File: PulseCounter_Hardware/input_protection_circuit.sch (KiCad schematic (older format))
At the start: 193 parts, among them J1 Conn_01x32_Male, U34 LTV-817, U35 LTV-817, U36 LTV-817, U37 LTV-817, U38 LTV-817, U39 LTV-817, U40 LTV-817, U41 LTV-817, U42 LTV-817, U43 LTV-817, U44 LTV-817, U45 LTV-817, U46 LTV-817, U47 LTV-817, U48 LTV-817, U49 LTV-817, U50 LTV-817, U51 LTV-817, U52 LTV-817, U53 LTV-817, U54 LTV-817, U55 LTV-817, U56 LTV-817, U57 LTV-817, U58 LTV-817, U59 LTV-817, U60 LTV-817, U61 LTV-817, U62 LTV-817, U63 LTV-817, U64 LTV-817, U65 LTV-817

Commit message: Starting with MCU
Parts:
- removed J1: Conn_01x32_Male, symbol Connector:Conn_01x32_Male
- added J1: Conn_01x33_Female, symbol Connector:Conn_01x33_Female
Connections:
- net CHANNEL_IN_0: now also J1.1 (Pin_1)
- net CHANNEL_IN_1: now also J1.2 (Pin_2)
- net CHANNEL_IN_10: now also J1.11 (Pin_11)
- net CHANNEL_IN_11: now also J1.12 (Pin_12)
- net CHANNEL_IN_12: now also J1.13 (Pin_13)
- net CHANNEL_IN_13: now also J1.14 (Pin_14)
- net CHANNEL_IN_14: now also J1.15 (Pin_15)
- net CHANNEL_IN_15: now also J1.16 (Pin_16)
- net CHANNEL_IN_16: now also J1.17 (Pin_17)
- net CHANNEL_IN_17: now also J1.18 (Pin_18)
- net CHANNEL_IN_18: now also J1.19 (Pin_19)
- net CHANNEL_IN_19: now also J1.20 (Pin_20)
- net CHANNEL_IN_2: now also J1.3 (Pin_3)
- net CHANNEL_IN_20: now also J1.21 (Pin_21)
- net CHANNEL_IN_21: now also J1.22 (Pin_22)
- net CHANNEL_IN_22: now also J1.23 (Pin_23)
- net CHANNEL_IN_23: now also J1.24 (Pin_24)
- net CHANNEL_IN_24: now also J1.25 (Pin_25)
- net CHANNEL_IN_25: now also J1.26 (Pin_26)
- net CHANNEL_IN_26: now also J1.27 (Pin_27)
- net CHANNEL_IN_27: now also J1.28 (Pin_28)
- net CHANNEL_IN_28: now also J1.29 (Pin_29)
- net CHANNEL_IN_29: now also J1.30 (Pin_30)
- net CHANNEL_IN_3: now also J1.4 (Pin_4)
- net CHANNEL_IN_30: now also J1.31 (Pin_31)
- net CHANNEL_IN_31: now also J1.32 (Pin_32)
- net CHANNEL_IN_4: now also J1.5 (Pin_5)
- net CHANNEL_IN_5: now also J1.6 (Pin_6)
- net CHANNEL_IN_6: now also J1.7 (Pin_7)
- net CHANNEL_IN_7: now also J1.8 (Pin_8)
- net CHANNEL_IN_8: now also J1.9 (Pin_9)
- net CHANNEL_IN_9: now also J1.10 (Pin_10)
- net OPTO_GND: now also J1.33 (Pin_33)
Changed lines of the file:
@@
 Wire Wire Line
 	13550 2400 13800 2400
-$Comp
-L Connector:Conn_01x32_Male J1
-U 1 1 5FA21E59
-P 14000 3900
-F 0 "J1" H 13972 3874 50  0000 R CNN
-F 1 "Conn_01x32_Male" H 13972 3783 50  0000 R CNN
-F 2 "" H 14000 3900 50  0001 C CNN
-F 3 "~" H 14000 3900 50  0001 C CNN
-	1    14000 3900
-	-1   0    0    -1
-$EndComp
 Wire Wire Line
 	13800 2500 13550 2500
@@
 Wire Notes Line
 	6850 800  6850 10750
+$Comp
+L Connector:Conn_01x33_Female J1
+U 1 1 5FD194EE
+P 14000 4000
+F 0 "J1" H 14028 4026 50  0000 L CNN
+F 1 "Conn_01x33_Female" H 14028 3935 50  0000 L CNN
+F 2 "" H 14000 4000 50  0001 C CNN
+F 3 "~" H 14000 4000 50  0001 C CNN
+	1    14000 4000
+	1    0    0    -1
+$EndComp
+Text Label 13550 5600 2    50   ~ 0
+OPTO_GND
+Wire Wire Line
+	13550 5600 13800 5600
+Text Label 13500 6050 2    50   ~ 0
+GND
+Text Label 13500 5950 2    50   ~ 0
+3V3
+Text HLabel 13700 6050 2    50   UnSpc ~ 0
+GND
+Text HLabel 13700 5950 2    50   UnSpc ~ 0
+3V3
+Wire Wire Line
+	13700 5950 13500 5950
+Wire Wire Line
+	13500 6050 13700 6050
 $EndSCHEMATC

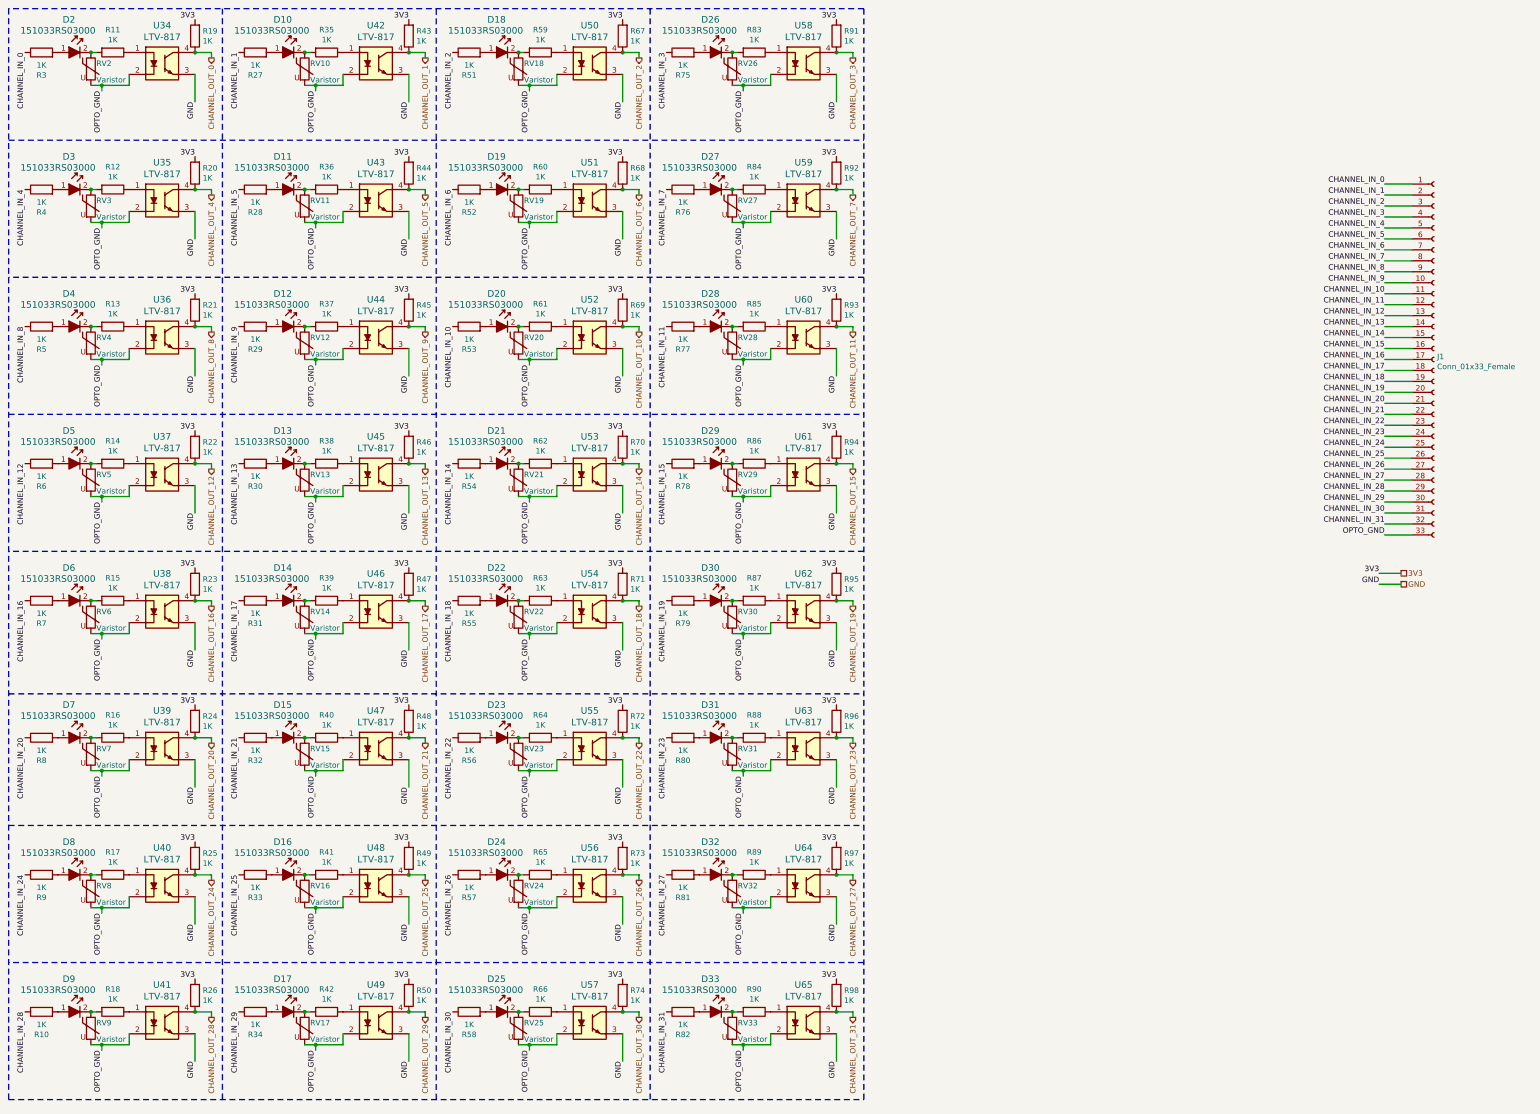
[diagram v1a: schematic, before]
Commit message: Added SPI flash, connected I2C, SPI
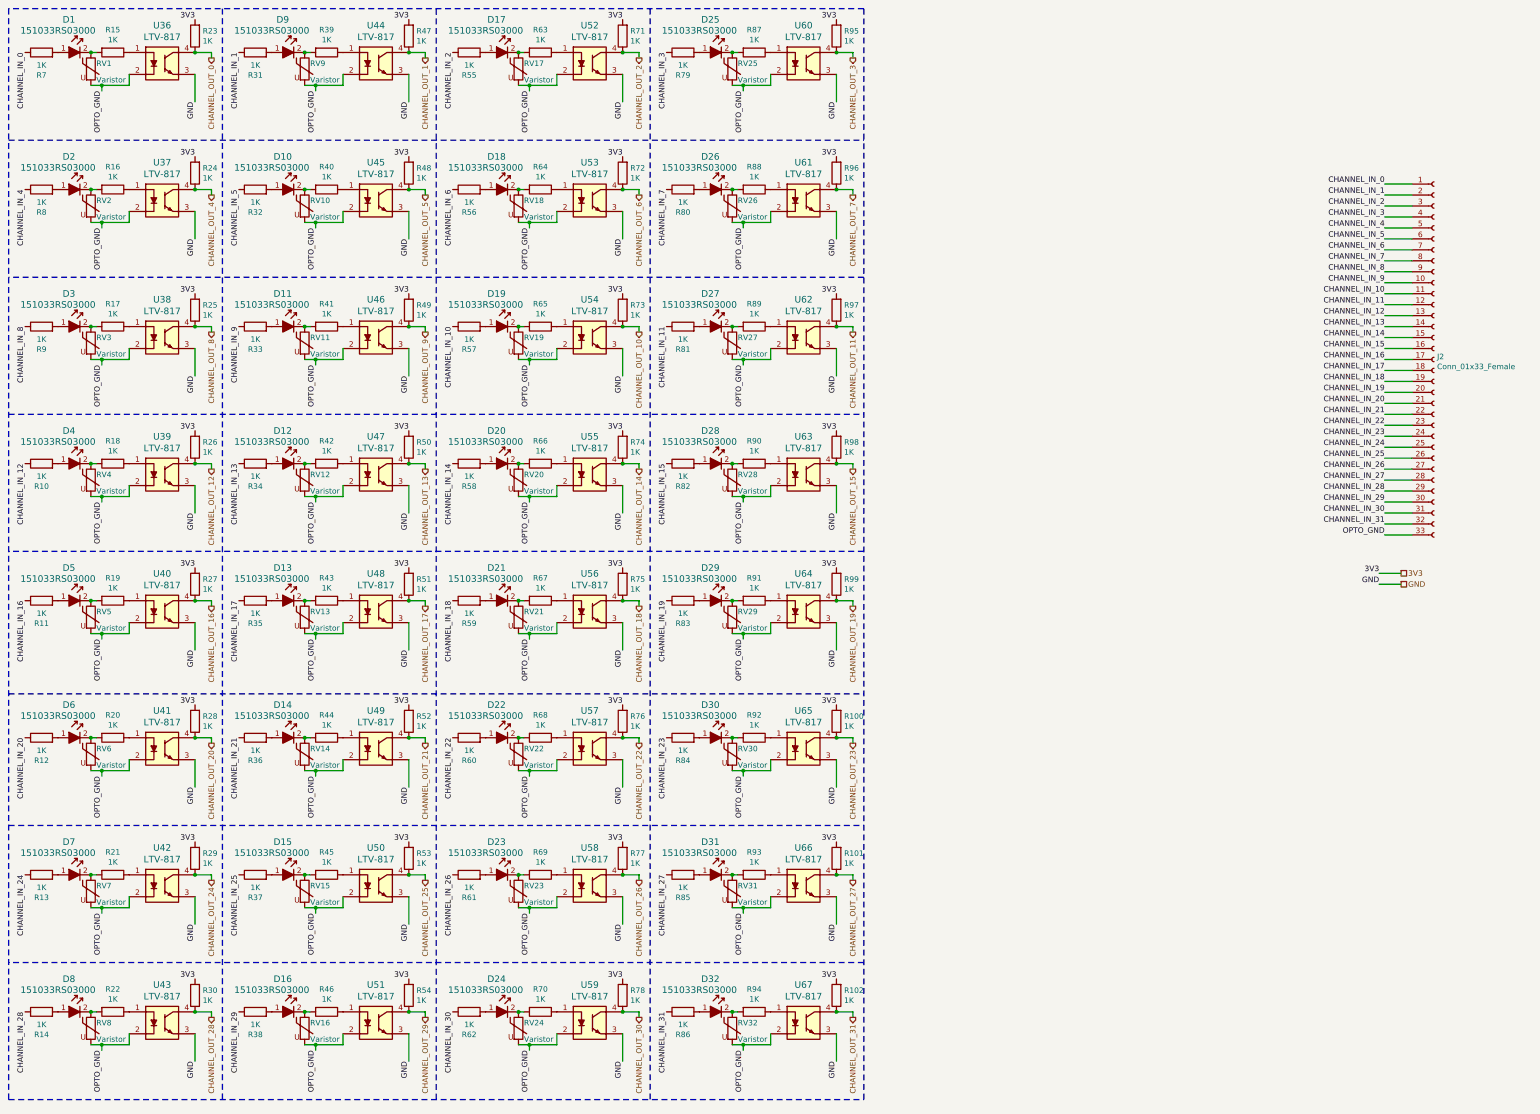
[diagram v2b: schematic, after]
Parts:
- renumbered D2 to D1, D11 to D10, D12 to D11, D13 to D12, D14 to D13, D15 to D14, D16 to D15, D17 to D16, D18 to D17, D19 to D18, D20 to D19, D3 to D2, D21 to D20, D22 to D21, D23 to D22, D24 to D23, D25 to D24, D26 to D25, D27 to D26, D28 to D27, D29 to D28, D30 to D29, D4 to D3, D31 to D30, D32 to D31, D33 to D32, D5 to D4, D6 to D5, D7 to D6, D8 to D7, D9 to D8, D10 to D9, J1 to J2, R6 to R10, R96 to R100, R97 to R101, R98 to R102, R7 to R11, R8 to R12, R9 to R13, R10 to R14, R11 to R15, R12 to R16, R13 to R17, R14 to R18, R15 to R19, R16 to R20, R17 to R21, R18 to R22, R19 to R23, R20 to R24, R21 to R25, R22 to R26, R23 to R27, R24 to R28, R25 to R29, R26 to R30, R27 to R31, R28 to R32, R29 to R33, R30 to R34, R31 to R35, R32 to R36, R33 to R37, R34 to R38, R35 to R39, R36 to R40, R37 to R41, R38 to R42, R39 to R43, R40 to R44, R41 to R45, R42 to R46, R43 to R47, R44 to R48, R45 to R49, R46 to R50, R47 to R51, R48 to R52, R49 to R53, R50 to R54, R51 to R55, R52 to R56, R53 to R57, R54 to R58, R55 to R59, R56 to R60, R57 to R61, R58 to R62, R59 to R63, R60 to R64, R61 to R65, R62 to R66, R63 to R67, R64 to R68, R65 to R69, R3 to R7, R66 to R70, R67 to R71, R68 to R72, R69 to R73, R70 to R74, R71 to R75, R72 to R76, R73 to R77, R74 to R78, R75 to R79, R4 to R8, R76 to R80, R77 to R81, R78 to R82, R79 to R83, R80 to R84, R81 to R85, R82 to R86, R83 to R87, R84 to R88, R85 to R89, R5 to R9, R86 to R90, R87 to R91, R88 to R92, R89 to R93, R90 to R94, R91 to R95, R92 to R96, R93 to R97, R94 to R98, R95 to R99, RV2 to RV1, RV11 to RV10, RV12 to RV11, RV13 to RV12, RV14 to RV13, RV15 to RV14, RV16 to RV15, RV17 to RV16, RV18 to RV17, RV19 to RV18, RV20 to RV19, RV3 to RV2, RV21 to RV20, RV22 to RV21, RV23 to RV22, RV24 to RV23, RV25 to RV24, RV26 to RV25, RV27 to RV26, RV28 to RV27, RV29 to RV28, RV30 to RV29, RV4 to RV3, RV31 to RV30, RV32 to RV31, RV33 to RV32, RV5 to RV4, RV6 to RV5, RV7 to RV6, RV8 to RV7, RV9 to RV8, RV10 to RV9, U34 to U36, U35 to U37, U36 to U38, U37 to U39, U38 to U40, U39 to U41, U40 to U42, U41 to U43, U42 to U44, U43 to U45, U44 to U46, U45 to U47, U46 to U48, U47 to U49, U48 to U50, U49 to U51, U50 to U52, U51 to U53, U52 to U54, U53 to U55, U54 to U56, U55 to U57, U56 to U58, U57 to U59, U58 to U60, U59 to U61, U60 to U62, U61 to U63, U62 to U64, U63 to U65, U64 to U66, U65 to U67

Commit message: Added correct varistor
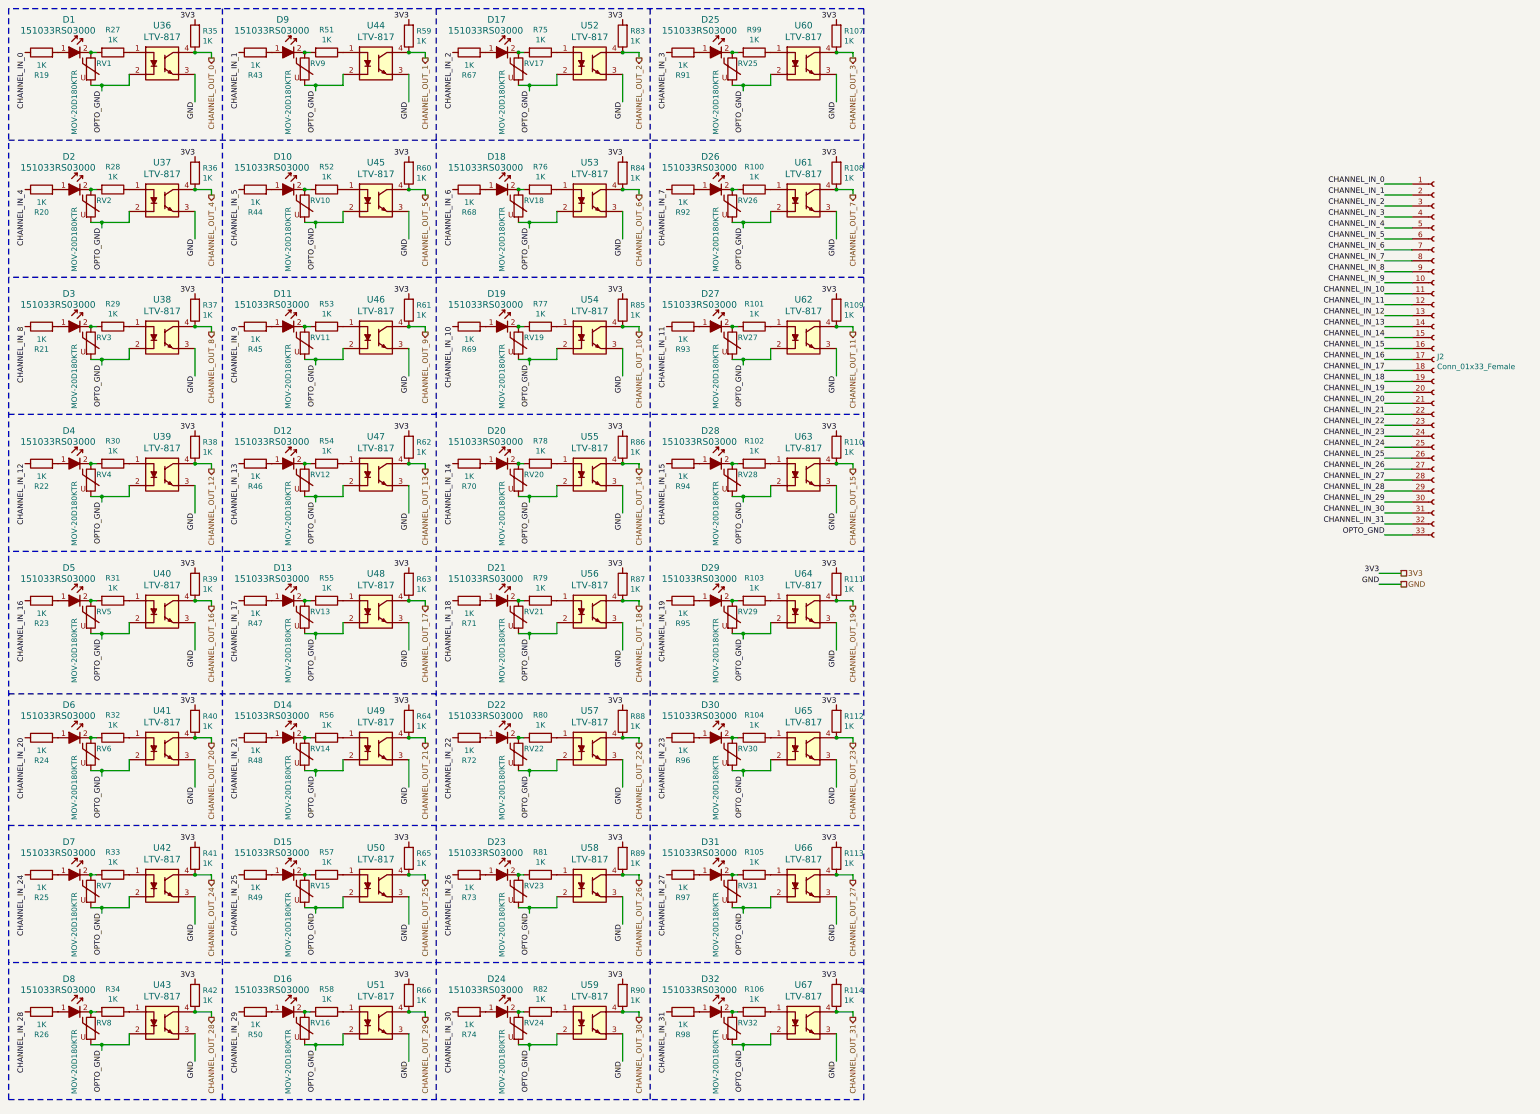
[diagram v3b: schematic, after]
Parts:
- J2: footprint (none) -> Connector_PinSocket_2.54mm:PinSocket_1x33_P2.54mm_Vertical
- R100: renamed from R88; footprint (none) -> Resistor_SMD:R_0603_1608Metric_Pad1.05x0.95mm_HandSolder
- R101: renamed from R89; footprint (none) -> Resistor_SMD:R_0603_1608Metric_Pad1.05x0.95mm_HandSolder
- R102: renamed from R90; footprint (none) -> Resistor_SMD:R_0603_1608Metric_Pad1.05x0.95mm_HandSolder
- R103: renamed from R91; footprint (none) -> Resistor_SMD:R_0603_1608Metric_Pad1.05x0.95mm_HandSolder
- R104: renamed from R92; footprint (none) -> Resistor_SMD:R_0603_1608Metric_Pad1.05x0.95mm_HandSolder
- R105: renamed from R93; footprint (none) -> Resistor_SMD:R_0603_1608Metric_Pad1.05x0.95mm_HandSolder
- R106: renamed from R94; footprint (none) -> Resistor_SMD:R_0603_1608Metric_Pad1.05x0.95mm_HandSolder
- R107: renamed from R95; footprint (none) -> Resistor_SMD:R_0603_1608Metric_Pad1.05x0.95mm_HandSolder
- R108: renamed from R96; footprint (none) -> Resistor_SMD:R_0603_1608Metric_Pad1.05x0.95mm_HandSolder
- R109: renamed from R97; footprint (none) -> Resistor_SMD:R_0603_1608Metric_Pad1.05x0.95mm_HandSolder
- R110: renamed from R98; footprint (none) -> Resistor_SMD:R_0603_1608Metric_Pad1.05x0.95mm_HandSolder
- R111: renamed from R99; footprint (none) -> Resistor_SMD:R_0603_1608Metric_Pad1.05x0.95mm_HandSolder
- R112: renamed from R100; footprint (none) -> Resistor_SMD:R_0603_1608Metric_Pad1.05x0.95mm_HandSolder
- R113: renamed from R101; footprint (none) -> Resistor_SMD:R_0603_1608Metric_Pad1.05x0.95mm_HandSolder
- R114: renamed from R102; footprint (none) -> Resistor_SMD:R_0603_1608Metric_Pad1.05x0.95mm_HandSolder
- R19: renamed from R7; footprint (none) -> Resistor_SMD:R_0603_1608Metric_Pad1.05x0.95mm_HandSolder
- R20: renamed from R8; footprint (none) -> Resistor_SMD:R_0603_1608Metric_Pad1.05x0.95mm_HandSolder
- R21: renamed from R9; footprint (none) -> Resistor_SMD:R_0603_1608Metric_Pad1.05x0.95mm_HandSolder
- R22: renamed from R10; footprint (none) -> Resistor_SMD:R_0603_1608Metric_Pad1.05x0.95mm_HandSolder
- R23: renamed from R11; footprint (none) -> Resistor_SMD:R_0603_1608Metric_Pad1.05x0.95mm_HandSolder
- R24: renamed from R12; footprint (none) -> Resistor_SMD:R_0603_1608Metric_Pad1.05x0.95mm_HandSolder
- R25: renamed from R13; footprint (none) -> Resistor_SMD:R_0603_1608Metric_Pad1.05x0.95mm_HandSolder
- R26: renamed from R14; footprint (none) -> Resistor_SMD:R_0603_1608Metric_Pad1.05x0.95mm_HandSolder
- R27: renamed from R15; footprint (none) -> Resistor_SMD:R_0603_1608Metric_Pad1.05x0.95mm_HandSolder
- R28: renamed from R16; footprint (none) -> Resistor_SMD:R_0603_1608Metric_Pad1.05x0.95mm_HandSolder
- R29: renamed from R17; footprint (none) -> Resistor_SMD:R_0603_1608Metric_Pad1.05x0.95mm_HandSolder
- R30: renamed from R18; footprint (none) -> Resistor_SMD:R_0603_1608Metric_Pad1.05x0.95mm_HandSolder
- R31: renamed from R19; footprint (none) -> Resistor_SMD:R_0603_1608Metric_Pad1.05x0.95mm_HandSolder
- R32: renamed from R20; footprint (none) -> Resistor_SMD:R_0603_1608Metric_Pad1.05x0.95mm_HandSolder
- R33: renamed from R21; footprint (none) -> Resistor_SMD:R_0603_1608Metric_Pad1.05x0.95mm_HandSolder
- R34: renamed from R22; footprint (none) -> Resistor_SMD:R_0603_1608Metric_Pad1.05x0.95mm_HandSolder
- R35: renamed from R23; footprint (none) -> Resistor_SMD:R_0603_1608Metric_Pad1.05x0.95mm_HandSolder
- R36: renamed from R24; footprint (none) -> Resistor_SMD:R_0603_1608Metric_Pad1.05x0.95mm_HandSolder
- R37: renamed from R25; footprint (none) -> Resistor_SMD:R_0603_1608Metric_Pad1.05x0.95mm_HandSolder
- R38: renamed from R26; footprint (none) -> Resistor_SMD:R_0603_1608Metric_Pad1.05x0.95mm_HandSolder
- R39: renamed from R27; footprint (none) -> Resistor_SMD:R_0603_1608Metric_Pad1.05x0.95mm_HandSolder
- R40: renamed from R28; footprint (none) -> Resistor_SMD:R_0603_1608Metric_Pad1.05x0.95mm_HandSolder
- R41: renamed from R29; footprint (none) -> Resistor_SMD:R_0603_1608Metric_Pad1.05x0.95mm_HandSolder
- R42: renamed from R30; footprint (none) -> Resistor_SMD:R_0603_1608Metric_Pad1.05x0.95mm_HandSolder
- R43: renamed from R31; footprint (none) -> Resistor_SMD:R_0603_1608Metric_Pad1.05x0.95mm_HandSolder
- R44: renamed from R32; footprint (none) -> Resistor_SMD:R_0603_1608Metric_Pad1.05x0.95mm_HandSolder
- R45: renamed from R33; footprint (none) -> Resistor_SMD:R_0603_1608Metric_Pad1.05x0.95mm_HandSolder
- R46: renamed from R34; footprint (none) -> Resistor_SMD:R_0603_1608Metric_Pad1.05x0.95mm_HandSolder
- R47: renamed from R35; footprint (none) -> Resistor_SMD:R_0603_1608Metric_Pad1.05x0.95mm_HandSolder
- R48: renamed from R36; footprint (none) -> Resistor_SMD:R_0603_1608Metric_Pad1.05x0.95mm_HandSolder
- R49: renamed from R37; footprint (none) -> Resistor_SMD:R_0603_1608Metric_Pad1.05x0.95mm_HandSolder
- R50: renamed from R38; footprint (none) -> Resistor_SMD:R_0603_1608Metric_Pad1.05x0.95mm_HandSolder
- R51: renamed from R39; footprint (none) -> Resistor_SMD:R_0603_1608Metric_Pad1.05x0.95mm_HandSolder
- R52: renamed from R40; footprint (none) -> Resistor_SMD:R_0603_1608Metric_Pad1.05x0.95mm_HandSolder
- R53: renamed from R41; footprint (none) -> Resistor_SMD:R_0603_1608Metric_Pad1.05x0.95mm_HandSolder
- R54: renamed from R42; footprint (none) -> Resistor_SMD:R_0603_1608Metric_Pad1.05x0.95mm_HandSolder
- R55: renamed from R43; footprint (none) -> Resistor_SMD:R_0603_1608Metric_Pad1.05x0.95mm_HandSolder
- R56: renamed from R44; footprint (none) -> Resistor_SMD:R_0603_1608Metric_Pad1.05x0.95mm_HandSolder
- R57: renamed from R45; footprint (none) -> Resistor_SMD:R_0603_1608Metric_Pad1.05x0.95mm_HandSolder
- R58: renamed from R46; footprint (none) -> Resistor_SMD:R_0603_1608Metric_Pad1.05x0.95mm_HandSolder
- R59: renamed from R47; footprint (none) -> Resistor_SMD:R_0603_1608Metric_Pad1.05x0.95mm_HandSolder
- R60: renamed from R48; footprint (none) -> Resistor_SMD:R_0603_1608Metric_Pad1.05x0.95mm_HandSolder
- R61: renamed from R49; footprint (none) -> Resistor_SMD:R_0603_1608Metric_Pad1.05x0.95mm_HandSolder
- R62: renamed from R50; footprint (none) -> Resistor_SMD:R_0603_1608Metric_Pad1.05x0.95mm_HandSolder
- R63: renamed from R51; footprint (none) -> Resistor_SMD:R_0603_1608Metric_Pad1.05x0.95mm_HandSolder
- R64: renamed from R52; footprint (none) -> Resistor_SMD:R_0603_1608Metric_Pad1.05x0.95mm_HandSolder
- R65: renamed from R53; footprint (none) -> Resistor_SMD:R_0603_1608Metric_Pad1.05x0.95mm_HandSolder
- R66: renamed from R54; footprint (none) -> Resistor_SMD:R_0603_1608Metric_Pad1.05x0.95mm_HandSolder
- R67: renamed from R55; footprint (none) -> Resistor_SMD:R_0603_1608Metric_Pad1.05x0.95mm_HandSolder
- R68: renamed from R56; footprint (none) -> Resistor_SMD:R_0603_1608Metric_Pad1.05x0.95mm_HandSolder
- R69: renamed from R57; footprint (none) -> Resistor_SMD:R_0603_1608Metric_Pad1.05x0.95mm_HandSolder
- R70: renamed from R58; footprint (none) -> Resistor_SMD:R_0603_1608Metric_Pad1.05x0.95mm_HandSolder
- R71: renamed from R59; footprint (none) -> Resistor_SMD:R_0603_1608Metric_Pad1.05x0.95mm_HandSolder
- R72: renamed from R60; footprint (none) -> Resistor_SMD:R_0603_1608Metric_Pad1.05x0.95mm_HandSolder
- R73: renamed from R61; footprint (none) -> Resistor_SMD:R_0603_1608Metric_Pad1.05x0.95mm_HandSolder
- R74: renamed from R62; footprint (none) -> Resistor_SMD:R_0603_1608Metric_Pad1.05x0.95mm_HandSolder
- R75: renamed from R63; footprint (none) -> Resistor_SMD:R_0603_1608Metric_Pad1.05x0.95mm_HandSolder
- R76: renamed from R64; footprint (none) -> Resistor_SMD:R_0603_1608Metric_Pad1.05x0.95mm_HandSolder
- R77: renamed from R65; footprint (none) -> Resistor_SMD:R_0603_1608Metric_Pad1.05x0.95mm_HandSolder
- R78: renamed from R66; footprint (none) -> Resistor_SMD:R_0603_1608Metric_Pad1.05x0.95mm_HandSolder
- R79: renamed from R67; footprint (none) -> Resistor_SMD:R_0603_1608Metric_Pad1.05x0.95mm_HandSolder
- R80: renamed from R68; footprint (none) -> Resistor_SMD:R_0603_1608Metric_Pad1.05x0.95mm_HandSolder
- R81: renamed from R69; footprint (none) -> Resistor_SMD:R_0603_1608Metric_Pad1.05x0.95mm_HandSolder
- R82: renamed from R70; footprint (none) -> Resistor_SMD:R_0603_1608Metric_Pad1.05x0.95mm_HandSolder
- R83: renamed from R71; footprint (none) -> Resistor_SMD:R_0603_1608Metric_Pad1.05x0.95mm_HandSolder
- R84: renamed from R72; footprint (none) -> Resistor_SMD:R_0603_1608Metric_Pad1.05x0.95mm_HandSolder
- R85: renamed from R73; footprint (none) -> Resistor_SMD:R_0603_1608Metric_Pad1.05x0.95mm_HandSolder
- R86: renamed from R74; footprint (none) -> Resistor_SMD:R_0603_1608Metric_Pad1.05x0.95mm_HandSolder
- R87: renamed from R75; footprint (none) -> Resistor_SMD:R_0603_1608Metric_Pad1.05x0.95mm_HandSolder
- R88: renamed from R76; footprint (none) -> Resistor_SMD:R_0603_1608Metric_Pad1.05x0.95mm_HandSolder
- R89: renamed from R77; footprint (none) -> Resistor_SMD:R_0603_1608Metric_Pad1.05x0.95mm_HandSolder
- R90: renamed from R78; footprint (none) -> Resistor_SMD:R_0603_1608Metric_Pad1.05x0.95mm_HandSolder
- R91: renamed from R79; footprint (none) -> Resistor_SMD:R_0603_1608Metric_Pad1.05x0.95mm_HandSolder
- R92: renamed from R80; footprint (none) -> Resistor_SMD:R_0603_1608Metric_Pad1.05x0.95mm_HandSolder
- R93: renamed from R81; footprint (none) -> Resistor_SMD:R_0603_1608Metric_Pad1.05x0.95mm_HandSolder
- R94: renamed from R82; footprint (none) -> Resistor_SMD:R_0603_1608Metric_Pad1.05x0.95mm_HandSolder
- R95: renamed from R83; footprint (none) -> Resistor_SMD:R_0603_1608Metric_Pad1.05x0.95mm_HandSolder
- R96: renamed from R84; footprint (none) -> Resistor_SMD:R_0603_1608Metric_Pad1.05x0.95mm_HandSolder
- R97: renamed from R85; footprint (none) -> Resistor_SMD:R_0603_1608Metric_Pad1.05x0.95mm_HandSolder
- R98: renamed from R86; footprint (none) -> Resistor_SMD:R_0603_1608Metric_Pad1.05x0.95mm_HandSolder
- R99: renamed from R87; footprint (none) -> Resistor_SMD:R_0603_1608Metric_Pad1.05x0.95mm_HandSolder
- RV1, RV10, RV11, RV12, RV13, RV14, RV15, RV16, RV17, RV18, RV19, RV2, RV20, RV21, RV22, RV23, RV24, RV25, RV26, RV27, RV28, RV29, RV3, RV30, RV31, RV32, RV4, RV5, RV6, RV7, RV8, RV9: value Varistor -> MOV-20D180KTR; footprint (none) -> Varistor:RV_Disc_D21.5mm_W4.3mm_P10mm; Digi-Key_PN (none) -> MOV-20D180KTRTR-ND
